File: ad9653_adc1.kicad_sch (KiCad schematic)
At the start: 20 parts, among them J701 142-0701-201, J702 142-0701-201, J703 142-0701-201, J704 142-0701-201, U701 AD9653BCPZ-125

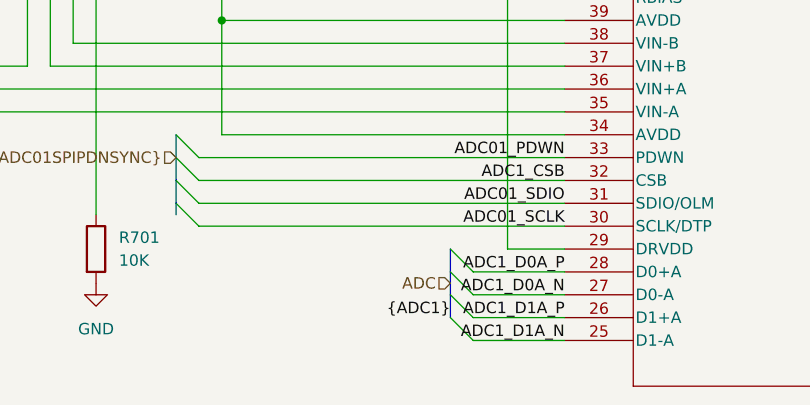
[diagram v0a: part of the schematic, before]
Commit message: Updates from Michal to fix ERC errors
Still lots of ERC warnings
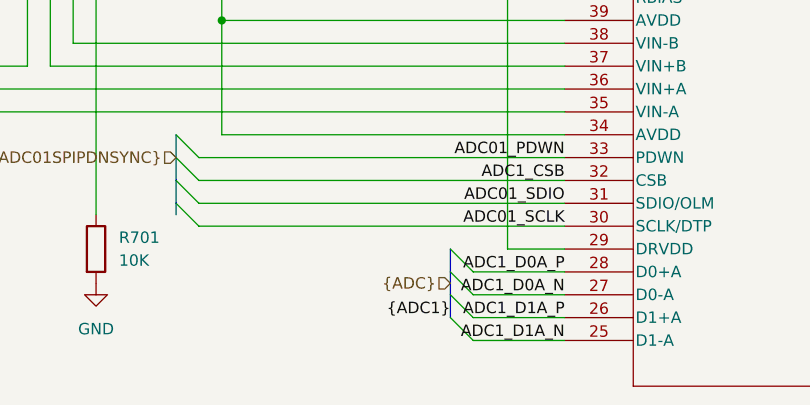
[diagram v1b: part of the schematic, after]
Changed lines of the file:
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@@
 		)
 	)
-	(hierarchical_label "ADC"
+	(hierarchical_label "{ADC}"
 		(shape input)
 		(at 115.57 142.24 180)

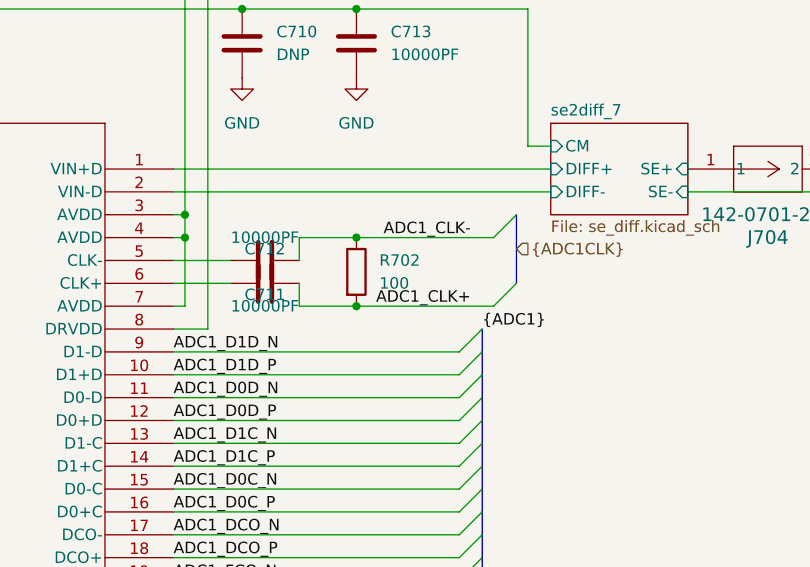
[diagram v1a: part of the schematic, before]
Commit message: Schematic Changes
Added Manufacturer/MPN/Description Fields to parts
Added libraries to project
Modified FMC schematic to use new symbol
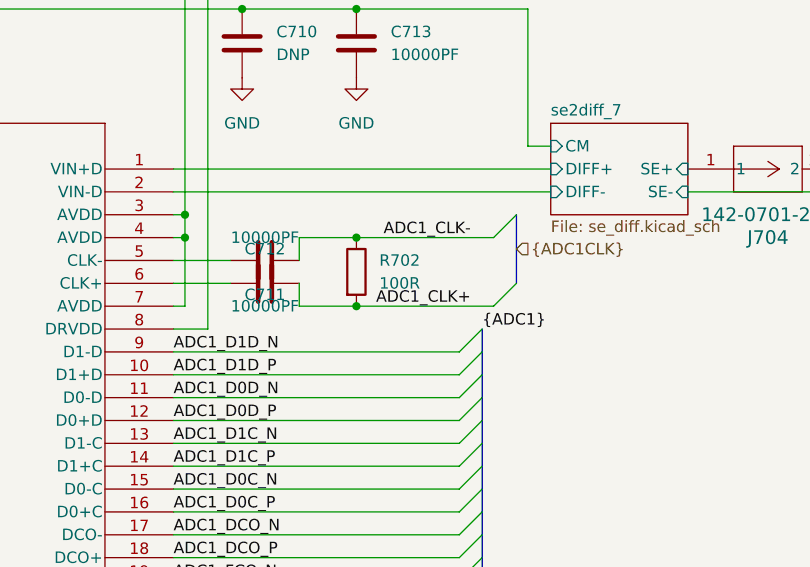
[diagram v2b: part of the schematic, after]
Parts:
- C701, C705: Manufacturer (none) -> TDK; Manufacturer Part Number (none) -> C1608X5R1A106M080AC
- C702, C704, C707, C708, C709: Manufacturer (none) -> Murata; Manufacturer Part Number (none) -> GRM155R61A104KA01D
- C703, C711, C712, C713: Manufacturer (none) -> TDK; Manufacturer Part Number (none) -> C1608C0G1E103J080AA
- C706: Manufacturer (none) -> Kyocera AVX; Manufacturer Part Number (none) -> F381A225MMA
- J701, J702, J703, J704: Manufacturer (none) -> Cinch; Manufacturer Part Number (none) -> 142-0701-201
- R701: Manufacturer (none) -> Vishay; Manufacturer Part Number (none) -> MCT0603MD1002DP500
- R702: value 100 -> 100R; Manufacturer (none) -> YAGEO; Manufacturer Part Number (none) -> RC0603FR-07100RL
- U701: Manufacturer (none) -> Analog Devices; Manufacturer Part Number (none) -> AD9653BCPZ-125

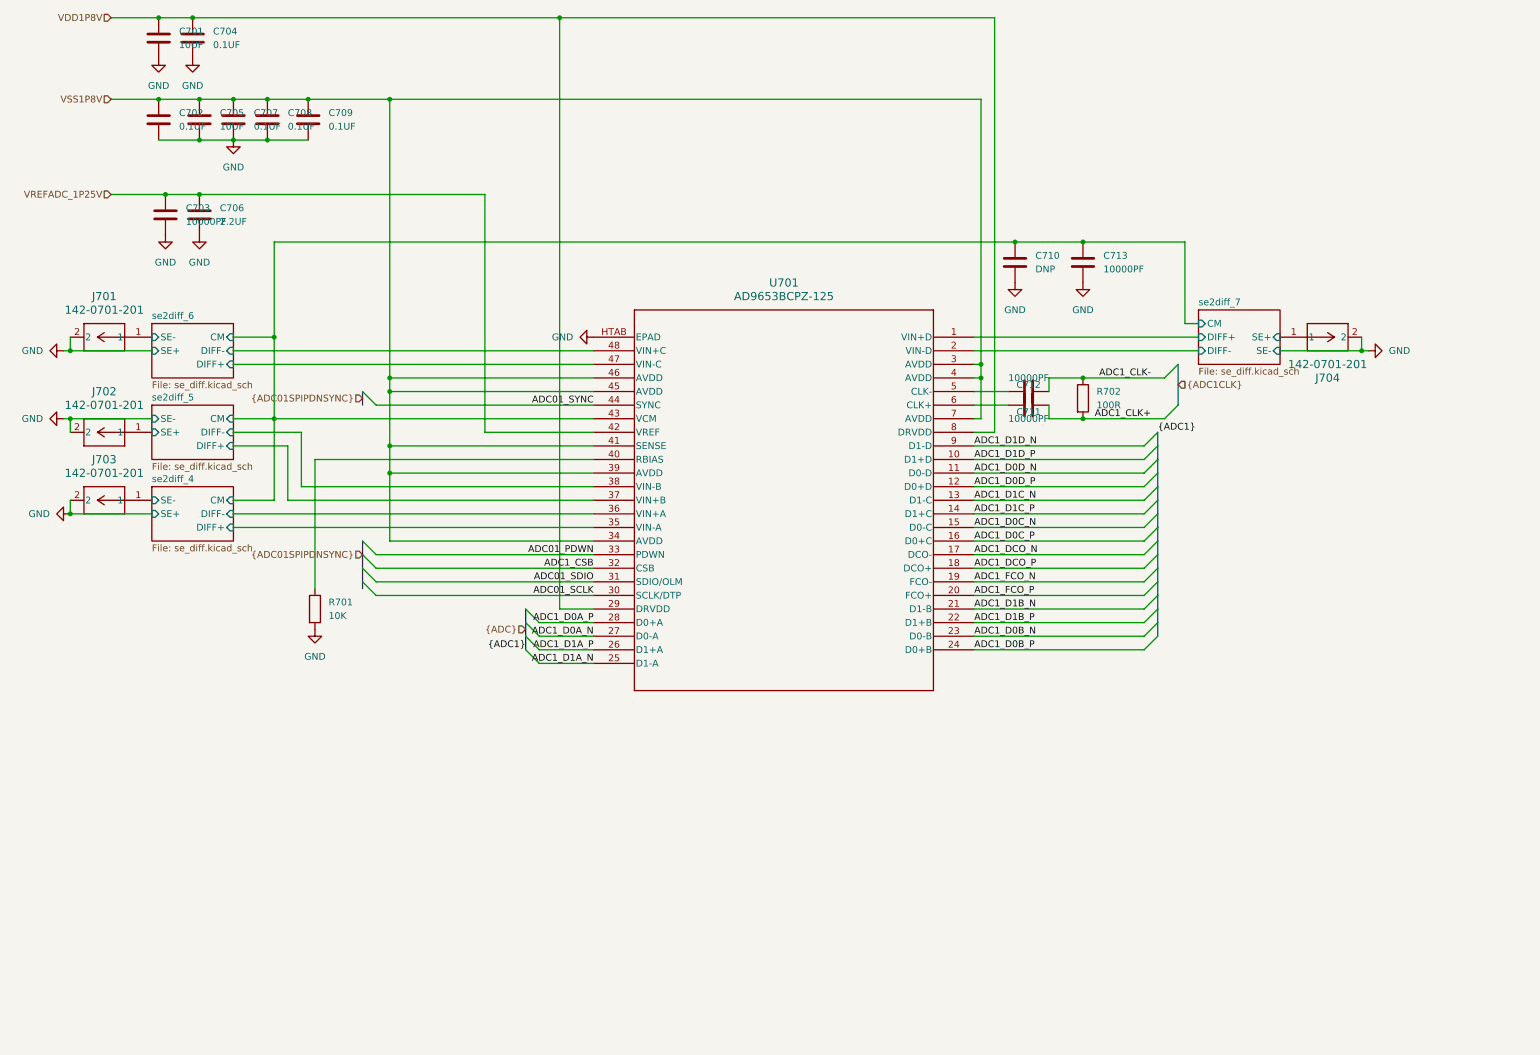
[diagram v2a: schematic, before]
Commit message: Schematics update
Cleaned up RF ADC and front end sections.
Verified that changes did not changes anything about the layout.
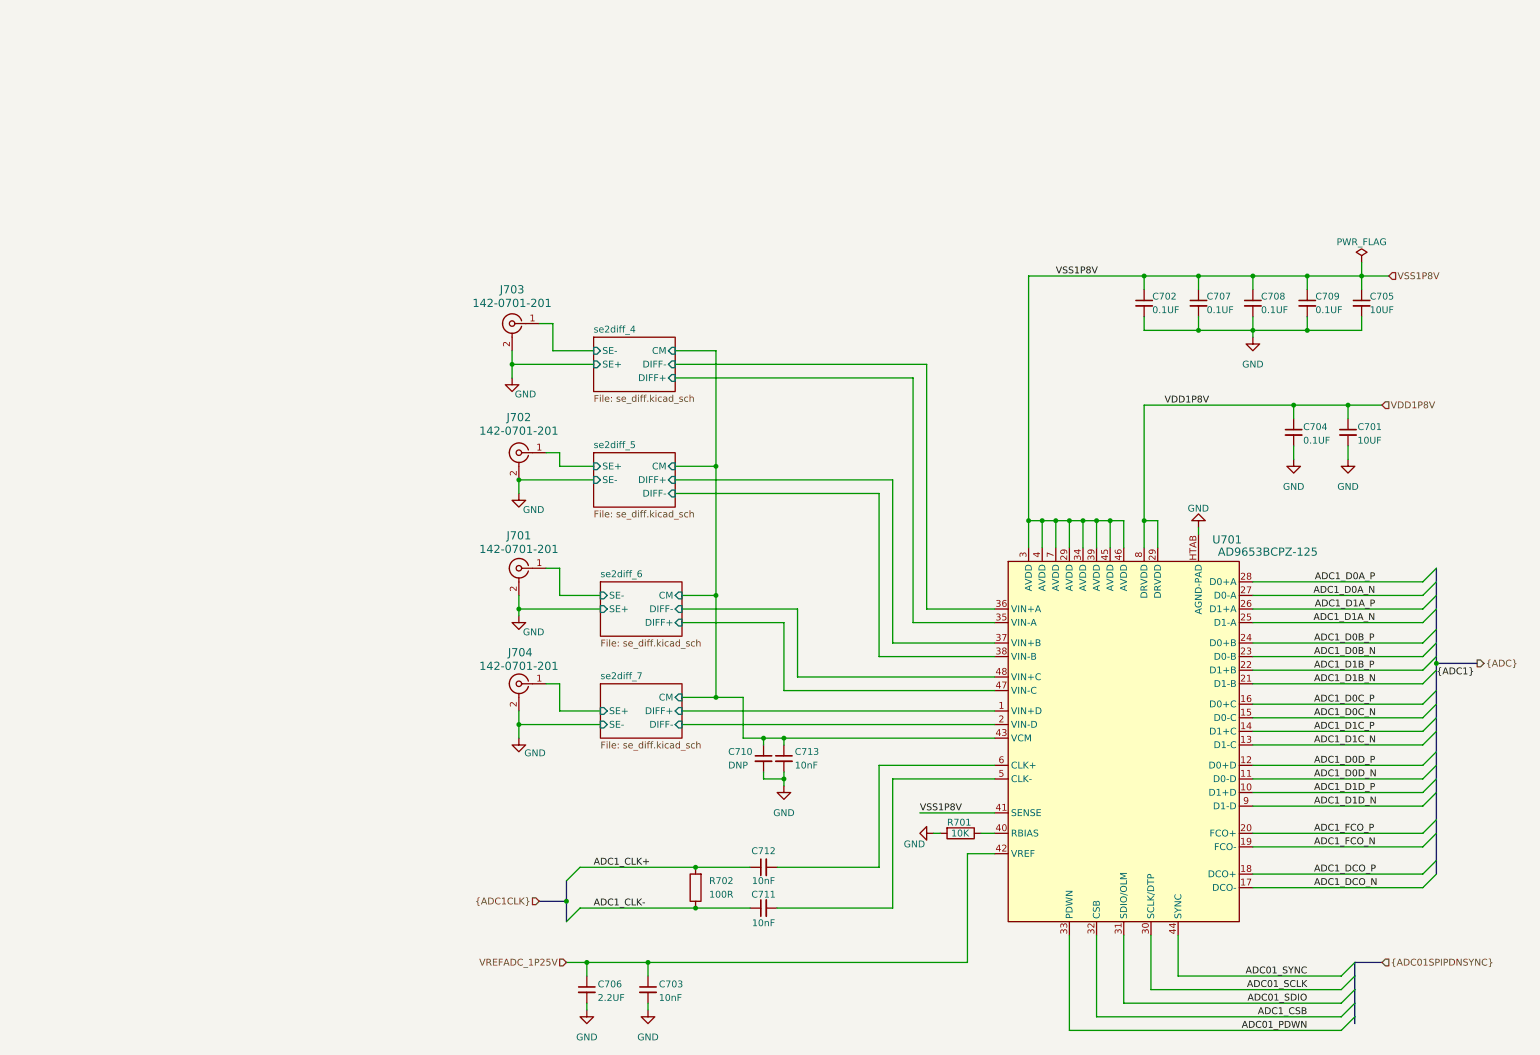
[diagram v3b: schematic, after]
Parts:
- C701, C702, C704, C705, C706, C707, C708, C709, C710: symbol Device:C -> Device:C_Small
- C703, C711, C712, C713: value 10000PF -> 10nF; symbol Device:C -> Device:C_Small
- J701, J702, J703, J704: symbol 001_symbol:142-0701-201_GH -> Zest_Custom:SMA_Coaxial
- U701: symbol 001_symbol:AD9653BCPZ-125 -> Zest_Custom:AD9653
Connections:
- net VSS1P8V: now also U701.29 (DRVDD)
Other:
- moved on the sheet: C701, C702, C703, C704, C705, C706, C707, C708, C709, C710, C711, C712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

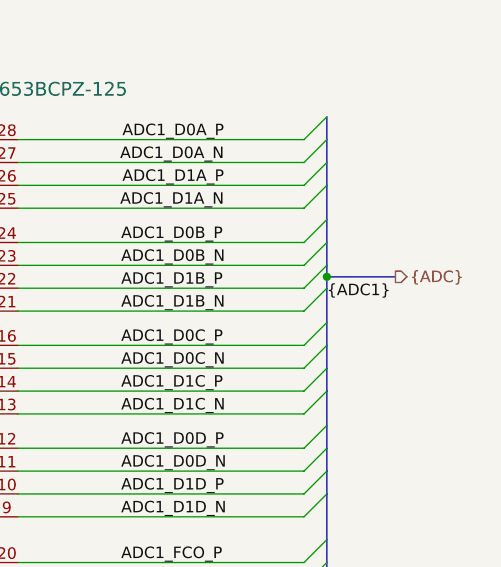
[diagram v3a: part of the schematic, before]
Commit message: Updated some Schematics
- updated slowmon schematic
- updated diff to se schematic
- cleaned up DRC/ERC errors
No changes were made that effected the PCB layout
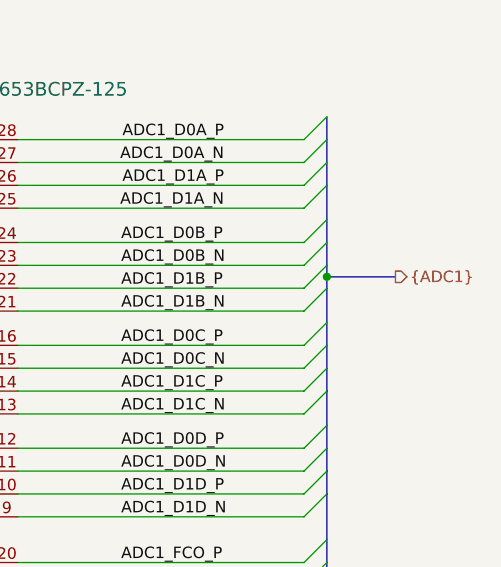
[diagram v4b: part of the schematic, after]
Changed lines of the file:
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@@
-		)
-	)
-	(label "{ADC1}"
-		(at 285.75 151.13 0)
-		(fields_autoplaced yes)
-		(effects
-			(font
-				(size 1.27 1.27)
-			)
-			(justify left bottom)
 		)
 	)
@@
 		)
 	)
-	(hierarchical_label "{ADC}"
+	(hierarchical_label "{ADC1}"
 		(shape output)
 		(at 293.37 148.59 0)

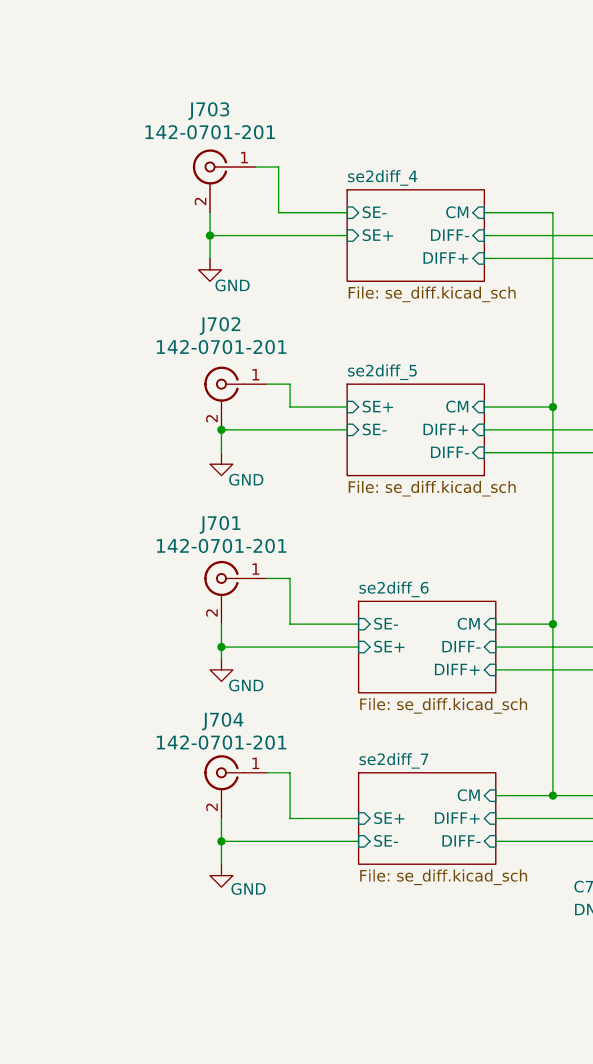
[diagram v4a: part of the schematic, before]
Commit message: Added DC blocking caps and minor layout tweaks
- Adding DC blocking input caps on ADC inputs

-Many minor changes to the layout listed below:
- General silkscreen tweak to avoid text over vias
-Adding pin1 markers on U1002, U2701,U2901,U3101,U3201,U3001,U903
-Adjusted pin1 indicator in footprint on U3002 to be close to part
-Adjusted the size of traces on U2301 to not have trace larger than pin
-Adjusted silkscreen of U1101 to not be underpart and moved pin 1 indicator closer
-Adjusted tracks around c901&R905 to go through center of pads
-Adjusted tracks around r2702&r2701 to go through center of pads
-Fixed some multi-via tracks to connect all vias around PMOD connector on top and in4 layers
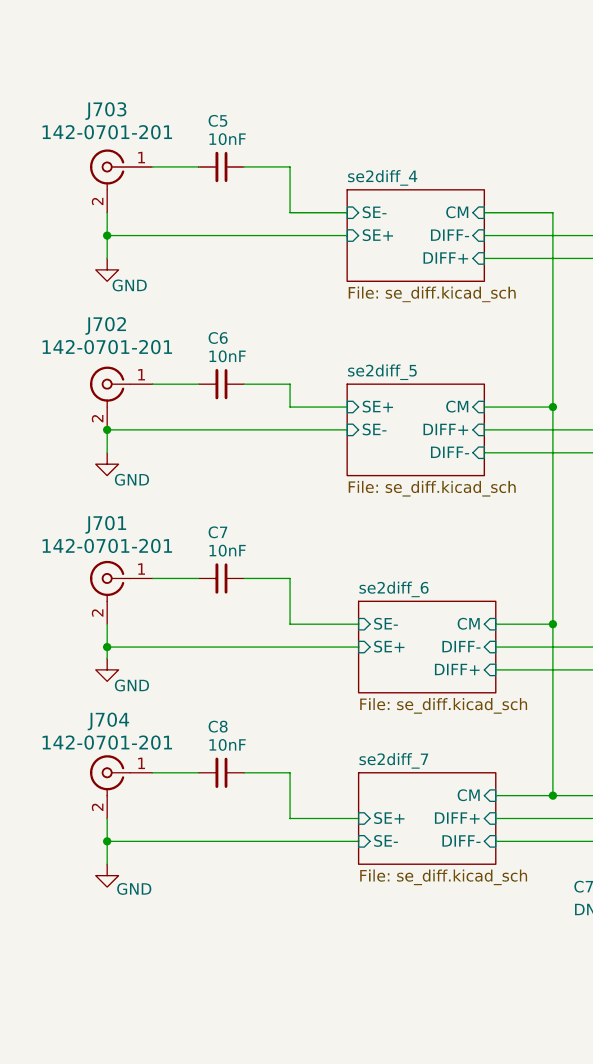
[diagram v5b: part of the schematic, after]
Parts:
- added C5, C6, C7, C8: 10nF, Capacitor_SMD:C_0603_1608Metric, symbol Device:C_Small
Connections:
- net se2diff_4/SE-: now also C5.1; no longer J703.1 (In)
- net se2diff_5/SE+: now also C6.1; no longer J702.1 (In)
- net se2diff_6/SE-: now also C7.1; no longer J701.1 (In)
- net se2diff_7/SE+: now also C8.1; no longer J704.1 (In)
- new net: C8.2, J704.1 (In)
- new net: C7.2, J701.1 (In)
- new net: C6.2, J702.1 (In)
- new net: C5.2, J703.1 (In)
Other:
- moved on the sheet: J701, J702, J703, J704

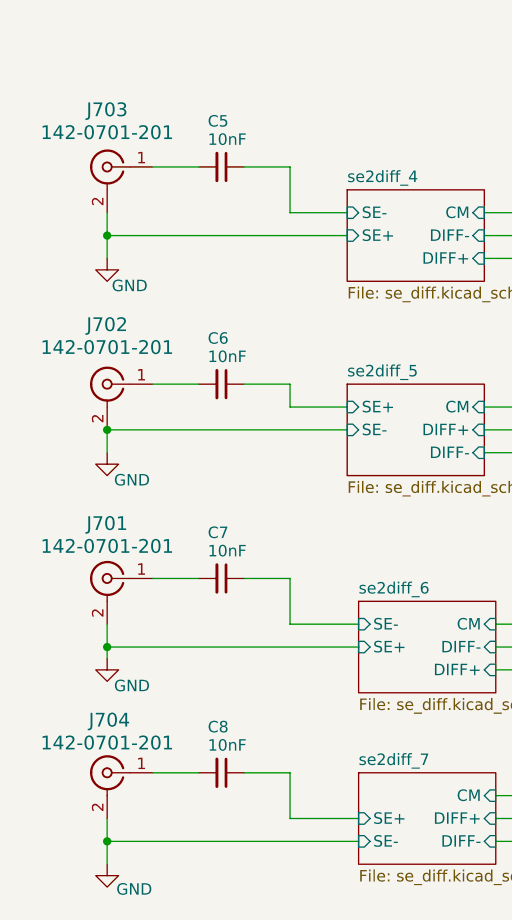
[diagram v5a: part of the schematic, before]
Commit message: Further Project cleanup
-Added BOM and fabrication files
-updated all documentation files
- Added suggested DC blocking cap at DAC outputs

-Set DRC to 5mil trace and space and fixed various violations detailed below
- Removed various small tracks overlapping IC pads on U2701,U2901,U3101,U3201
- Spaced vias 5 mil apart around U701, U201, 1201
- Moved LMK_CLKout3 pair on In4 layer away from PMOD1_1 pin
- adjusted track into pin47 on U701 to clear pin 48
- adjusted trace under U903 to give more room from ground pads/vias
- spaced out vias around pins45/46 of U201

-Many tweak to trace to go through the center of pad throughout the design
-An example is the trace around C3005
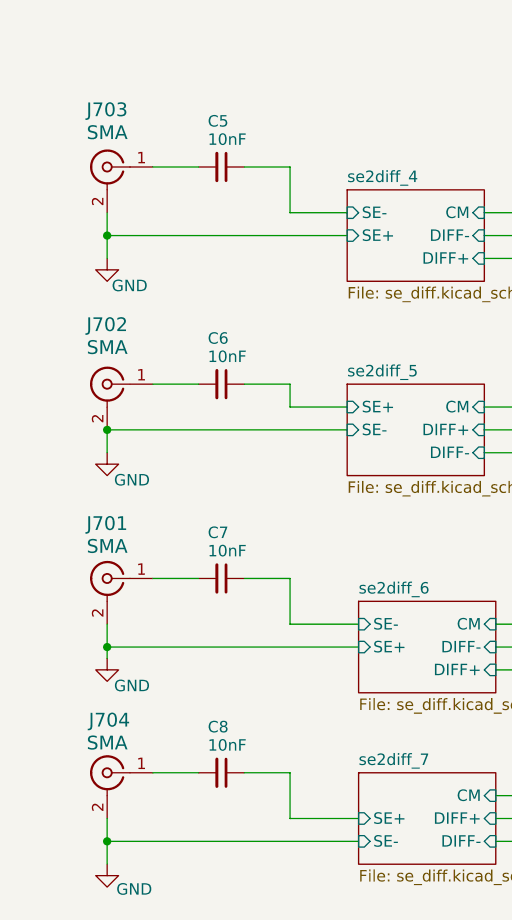
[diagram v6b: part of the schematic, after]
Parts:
- J701, J702, J703, J704: value 142-0701-201 -> SMA
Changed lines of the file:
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@@
 			)
 		)
-		(property "Value" "142-0701-201"
+		(property "Value" "SMA"
 			(at 101.6 149.098 0)
 			(effects
@@
 			)
 		)
-		(property "Value" "142-0701-201"
+		(property "Value" "SMA"
 			(at 101.6 127.254 0)
 			(effects
@@
 			)
 		)
-		(property "Value" "142-0701-201"
+		(property "Value" "SMA"
 			(at 101.6 105.156 0)
 			(effects
@@
 			)
 		)
-		(property "Description" "CAP CER 10nF 25V C0G 0603"
+		(property "Description" "CAP CER 10000PF 25V C0G 0603"
 			(at 163.83 166.37 0)
 			(effects
@@
 			)
 		)
-		(property "Value" "142-0701-201"
+		(property "Value" "SMA"
 			(at 101.6 81.28 0)
 			(effects
@@
 			)
 		)
-		(property "Description" "CAP CER 10nF 25V C0G 0603"
+		(property "Description" "CAP CER 10000PF 25V C0G 0603"
 			(at 160.02 186.69 0)
 			(effects
@@
 			)
 		)
-		(property "Description" "CAP CER 10nF 25V C0G 0603"
+		(property "Description" "CAP CER 10000PF 25V C0G 0603"
 			(at 114.3 152.4 0)
 			(effects
@@
 			)
 		)
-		(property "Description" "CAP CER 10nF 25V C0G 0603"
+		(property "Description" "CAP CER 10000PF 25V C0G 0603"
 			(at 114.3 130.81 0)
 			(effects
@@
 			)
 		)
-		(property "Description" "CAP CER 10nF 25V C0G 0603"
+		(property "Description" "CAP CER 10000PF 25V C0G 0603"
 			(at 114.3 85.09 0)
 			(effects
@@
 			)
 		)
-		(property "Description" "CAP CER 10nF 25V C0G 0603"
+		(property "Description" "CAP CER 10000PF 25V C0G 0603"
 			(at 160.02 194.31 0)
 			(effects
@@
 			)
 		)
-		(property "Description" "CAP CER 10nF 25V C0G 0603"
+		(property "Description" "CAP CER 10000PF 25V C0G 0603"
 			(at 138.43 209.55 0)
 			(effects
@@
 			)
 		)
-		(property "Description" "CAP CER 10nF 25V C0G 0603"
+		(property "Description" "CAP CER 10000PF 25V C0G 0603"
 			(at 114.3 109.22 0)
 			(effects
